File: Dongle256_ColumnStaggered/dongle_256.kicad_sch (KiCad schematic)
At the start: 66 parts, among them J1 Conn_01x02_Male, SW1 GateronLP, SW10 GateronLP, SW11 GateronLP, SW12 GateronLP, SW13 GateronLP, SW14 GateronLP, SW15 GateronLP, SW16 GateronLP, SW17 GateronLP, SW18 GateronLP, SW19 GateronLP, SW2 GateronLP, SW20 GateronLP, SW21 GateronLP, SW22 GateronLP, SW23 GateronLP, SW24 GateronLP, SW25 GateronLP, SW26 GateronLP, SW27 GateronLP, SW28 GateronLP, SW29 GateronLP, SW3 GateronLP, SW30 GateronLP, SW31 SW_DIP_x03, SW4 GateronLP, SW5 GateronLP, SW6 GateronLP, SW7 GateronLP, SW8 GateronLP, SW9 GateronLP, U1 NRF52840-DONGLE, U2 NRF52840-DONGLE

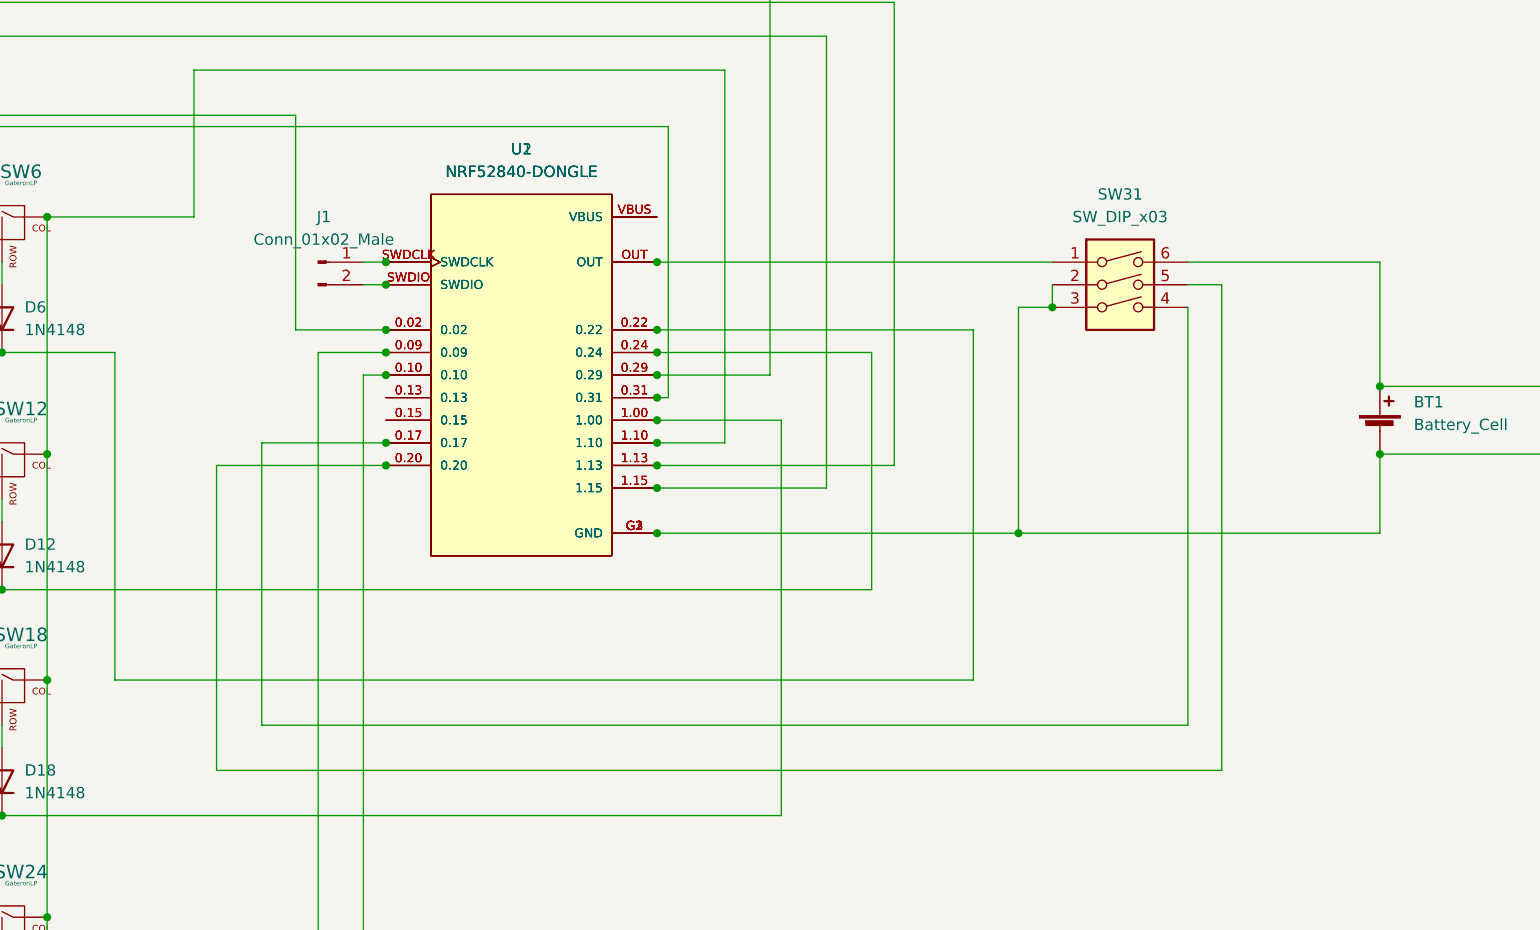
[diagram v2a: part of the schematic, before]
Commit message: Update flashing pads and redo the status switch.
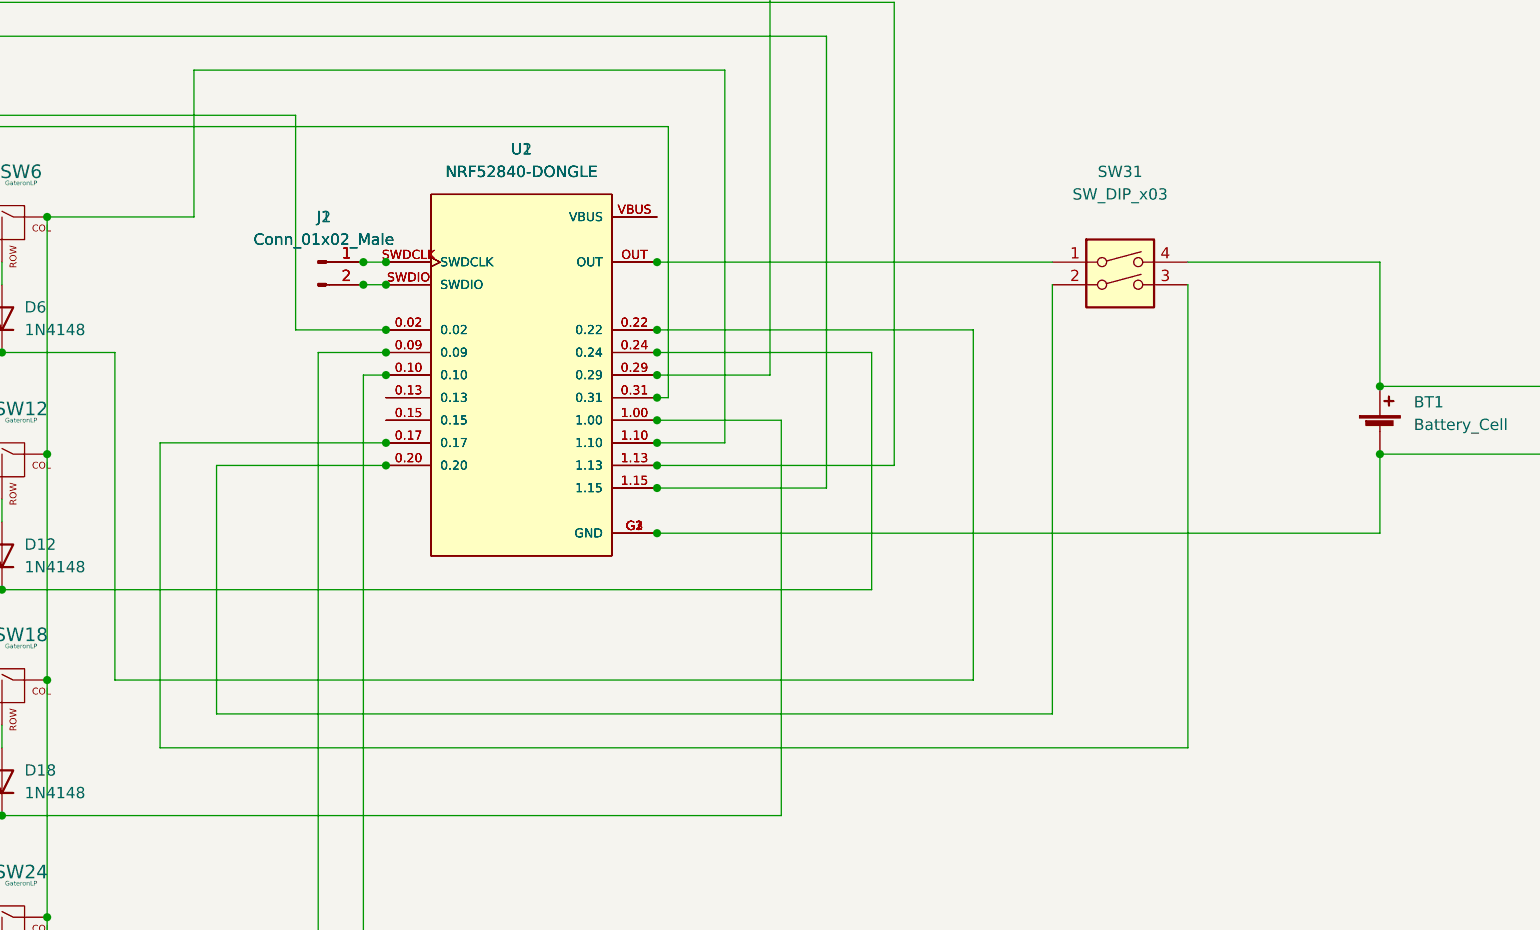
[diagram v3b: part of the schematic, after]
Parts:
- added J2: Conn_01x02_Male, Connector_PinHeader_2.54mm:PinHeader_1x02_P2.54mm_Vertical, symbol Connector:Conn_01x02_Male
- SW31: symbol Switch:SW_DIP_x03 -> Switch:SW_DIP_x02
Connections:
- net at BT1.1 (+), BT2.1 (+): now also SW31.4; no longer SW31.6
- net at BT1.2 (-), BT2.2 (-), U1.G1 (GND)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: no longer SW31.2, SW31.3
- net at U1.0.17, U2.0.17: now also SW31.3; no longer SW31.4
- net at U1.0.20, U2.0.20: now also SW31.2; no longer SW31.5
- net at J1.1 (Pin_1), U1.SWDCLK, U2.SWDCLK: now also J2.1 (Pin_1)
- net at J1.2 (Pin_2), U1.SWDIO, U2.SWDIO: now also J2.2 (Pin_2)
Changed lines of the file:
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@@
   (junction (at 177.8 45.72) (diameter 0) (color 0 0 0 0)
   )
+  (junction (at 175.26 35.56) (diameter 0) (color 0 0 0 0)
+  )
   (junction (at 48.26 27.94) (diameter 0) (color 0 0 0 0)
   )
@@
   (junction (at 208.28 50.8) (diameter 0) (color 0 0 0 0)
   )
+  (junction (at 175.26 33.02) (diameter 0) (color 0 0 0 0)
+  )
   (junction (at 134.62 95.25) (diameter 0) (color 0 0 0 0)
   )
@@
   (junction (at 97.79 69.85) (diameter 0) (color 0 0 0 0)
   )
-  (junction (at 248.92 63.5) (diameter 0) (color 0 0 0 0)
-  )
   (junction (at 60.96 148.59) (diameter 0) (color 0 0 0 0)
   )
@@
   (junction (at 115.57 69.85) (diameter 0) (color 0 0 0 0)
   )
-  (junction (at 252.73 38.1) (diameter 0) (color 0 0 0 0)
-  )
   (junction (at 139.7 106.68) (diameter 0) (color 0 0 0 0)
   )
@@
     (stroke (width 0) (type default) (color 0 0 0 0))
   )
-  (wire (pts (xy 163.83 85.09) (xy 163.83 53.34))
+  (wire (pts (xy 152.4 87.63) (xy 152.4 53.34))
     (stroke (width 0) (type default) (color 0 0 0 0))
   )
@@
     (stroke (width 0) (type default) (color 0 0 0 0))
   )
-  (wire (pts (xy 267.97 85.09) (xy 267.97 38.1))
-    (stroke (width 0) (type default) (color 0 0 0 0))
-  )
   (wire (pts (xy 134.62 148.59) (xy 175.26 148.59))
     (stroke (width 0) (type default) (color 0 0 0 0))
@@
     (stroke (width 0) (type default) (color 0 0 0 0))
   )
-  (wire (pts (xy 248.92 38.1) (xy 248.92 63.5))
+  (wire (pts (xy 267.97 33.02) (xy 289.56 33.02))
     (stroke (width 0) (type default) (color 0 0 0 0))
   )
@@
     (stroke (width 0) (type default) (color 0 0 0 0))
   )
-  (wire (pts (xy 267.97 35.56) (xy 271.78 35.56))
-    (stroke (width 0) (type default) (color 0 0 0 0))
-  )
   (wire (pts (xy 115.57 43.18) (xy 134.62 43.18))
     (stroke (width 0) (type default) (color 0 0 0 0))
@@
     (stroke (width 0) (type default) (color 0 0 0 0))
   )
-  (wire (pts (xy 208.28 63.5) (xy 248.92 63.5))
-    (stroke (width 0) (type default) (color 0 0 0 0))
-  )
   (wire (pts (xy 66.04 1.27) (xy 220.98 1.27))
     (stroke (width 0) (type default) (color 0 0 0 0))
@@
     (stroke (width 0) (type default) (color 0 0 0 0))
   )
-  (wire (pts (xy 163.83 85.09) (xy 267.97 85.09))
+  (wire (pts (xy 152.4 87.63) (xy 267.97 87.63))
     (stroke (width 0) (type default) (color 0 0 0 0))
   )
@@
     (stroke (width 0) (type default) (color 0 0 0 0))
   )
-  (wire (pts (xy 271.78 35.56) (xy 271.78 90.17))
-    (stroke (width 0) (type default) (color 0 0 0 0))
-  )
   (wire (pts (xy 102.87 80.01) (xy 102.87 106.68))
     (stroke (width 0) (type default) (color 0 0 0 0))
@@
     (stroke (width 0) (type default) (color 0 0 0 0))
   )
-  (wire (pts (xy 248.92 63.5) (xy 289.56 63.5))
+  (wire (pts (xy 208.28 63.5) (xy 289.56 63.5))
     (stroke (width 0) (type default) (color 0 0 0 0))
   )
@@
     (stroke (width 0) (type default) (color 0 0 0 0))
   )
-  (wire (pts (xy 252.73 38.1) (xy 248.92 38.1))
-    (stroke (width 0) (type default) (color 0 0 0 0))
-  )
   (wire (pts (xy 170.18 121.92) (xy 170.18 43.18))
     (stroke (width 0) (type default) (color 0 0 0 0))
@@
     (stroke (width 0) (type default) (color 0 0 0 0))
   )
+  (wire (pts (xy 252.73 35.56) (xy 252.73 83.82))
+    (stroke (width 0) (type default) (color 0 0 0 0))
+  )
   (wire (pts (xy 120.65 3.81) (xy 120.65 27.94))
     (stroke (width 0) (type default) (color 0 0 0 0))
@@
     (stroke (width 0) (type default) (color 0 0 0 0))
   )
-  (wire (pts (xy 158.75 55.88) (xy 158.75 90.17))
+  (wire (pts (xy 158.75 55.88) (xy 158.75 83.82))
     (stroke (width 0) (type default) (color 0 0 0 0))
   )
@@
     (stroke (width 0) (type default) (color 0 0 0 0))
   )
-  (wire (pts (xy 163.83 53.34) (xy 177.8 53.34))
-    (stroke (width 0) (type default) (color 0 0 0 0))
-  )
-  (wire (pts (xy 158.75 90.17) (xy 271.78 90.17))
+  (wire (pts (xy 267.97 87.63) (xy 267.97 35.56))
+    (stroke (width 0) (type default) (color 0 0 0 0))
+  )
+  (wire (pts (xy 152.4 53.34) (xy 177.8 53.34))
+    (stroke (width 0) (type default) (color 0 0 0 0))
+  )
+  (wire (pts (xy 158.75 83.82) (xy 252.73 83.82))
     (stroke (width 0) (type default) (color 0 0 0 0))
   )
@@
   )
   (wire (pts (xy 43.18 85.09) (xy 43.18 87.63))
-    (stroke (width 0) (type default) (color 0 0 0 0))
-  )
-  (wire (pts (xy 267.97 33.02) (xy 289.56 33.02))
-    (stroke (width 0) (type default) (color 0 0 0 0))
-  )
-  (wire (pts (xy 252.73 35.56) (xy 252.73 38.1))
     (stroke (width 0) (type default) (color 0 0 0 0))
   )
@@
     (pin "2")
   )
-  (symbol (lib_id "Switch:SW_DIP_x03") (at 260.35 38.1 0) (unit 1)
-    (in_bom yes) (on_board yes) (fields_autoplaced)
-    (property "Reference" "SW31" (id 0) (at 260.35 25.4 0))
-    (property "Value" "SW_DIP_x03" (id 1) (at 260.35 27.94 0))
-    (property "Footprint" "Button_Switch_THT:SW_DIP_SPSTx03_Slide_9.78x9.8mm_W7.62mm_P2.54mm" (id 2) (at 260.35 38.1 0)
-      (effects (font (size 1.27 1.27)) hide)
-    )
-    (property "Datasheet" "~" (id 3) (at 260.35 38.1 0)
+  (symbol (lib_id "Switch:SW_DIP_x02") (at 260.35 35.56 0) (unit 1)
+    (in_bom yes) (on_board yes) (fields_autoplaced)
+    (property "Reference" "SW31" (id 0) (at 260.35 22.86 0))
+    (property "Value" "SW_DIP_x03" (id 1) (at 260.35 25.4 0))
+    (property "Footprint" "Button_Switch_THT:SW_DIP_SPSTx03_Slide_9.78x9.8mm_W7.62mm_P2.54mm" (id 2) (at 260.35 35.56 0)
+      (effects (font (size 1.27 1.27)) hide)
+    )
+    (property "Datasheet" "~" (id 3) (at 260.35 35.56 0)
       (effects (font (size 1.27 1.27)) hide)
     )
@@
     (pin "3")
     (pin "4")
-    (pin "5")
-    (pin "6")
   )
   (symbol (lib_id "Diode:1N4148") (at 134.62 66.04 90) (unit 1)
@@
     (pin "2")
   )
+  (symbol (lib_id "Connector:Conn_01x02_Male") (at 170.18 33.02 0) (unit 1)
+    (in_bom yes) (on_board yes) (fields_autoplaced)
+    (property "Reference" "J2" (id 0) (at 170.815 27.94 0))
+    (property "Value" "Conn_01x02_Male" (id 1) (at 170.815 30.48 0))
+    (property "Footprint" "Connector_PinHeader_2.54mm:PinHeader_1x02_P2.54mm_Vertical" (id 2) (at 170.18 33.02 0)
+      (effects (font (size 1.27 1.27)) hide)
+    )
+    (property "Datasheet" "~" (id 3) (at 170.18 33.02 0)
+      (effects (font (size 1.27 1.27)) hide)
+    )
+    (pin "1")
+    (pin "2")
+  )
   (symbol (lib_id "Diode:1N4148") (at 134.62 39.37 90) (unit 1)
     (in_bom yes) (on_board yes) (fields_autoplaced)
@@
       (reference "J1") (unit 1) (value "Conn_01x02_Male") (footprint "Connector_PinHeader_2.54mm:PinHeader_1x02_P2.54mm_Vertical")
     )
+    (path "/877fd0e1-439d-4ba8-8e8d-50a7938db2ab"
+      (reference "J2") (unit 1) (value "Conn_01x02_Male") (footprint "Connector_PinHeader_2.54mm:PinHeader_1x02_P2.54mm_Vertical")
+    )
     (path "/68306db6-e9fe-420d-a5be-029e7f2a4533"
